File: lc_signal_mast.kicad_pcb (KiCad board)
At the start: 2 copper layers, 100.4 x 93.2 mm, 64 parts, among them J1 Conn_01x04_Male, J2 Conn_01x04_Male

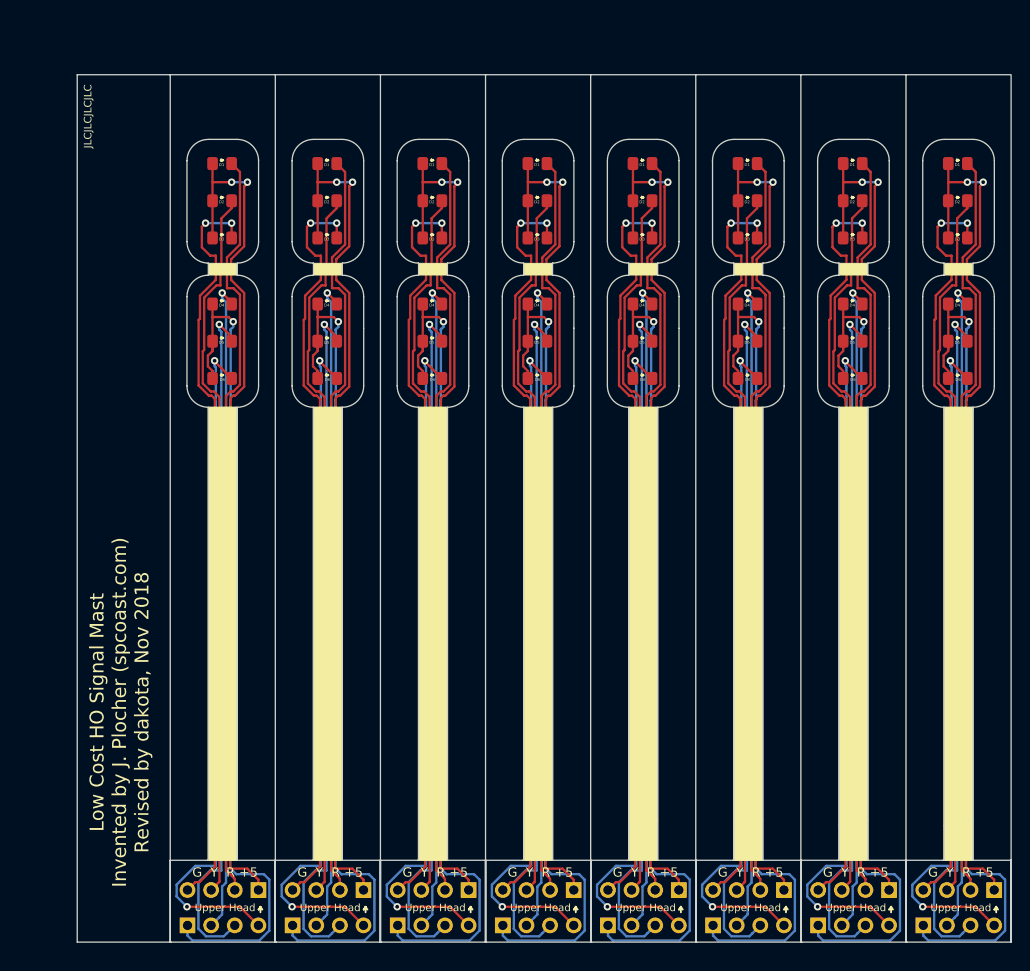
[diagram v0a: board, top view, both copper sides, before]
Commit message: Stagger headers on the bottom; swap R/G LED footprints.
Fixes #6 and #9.
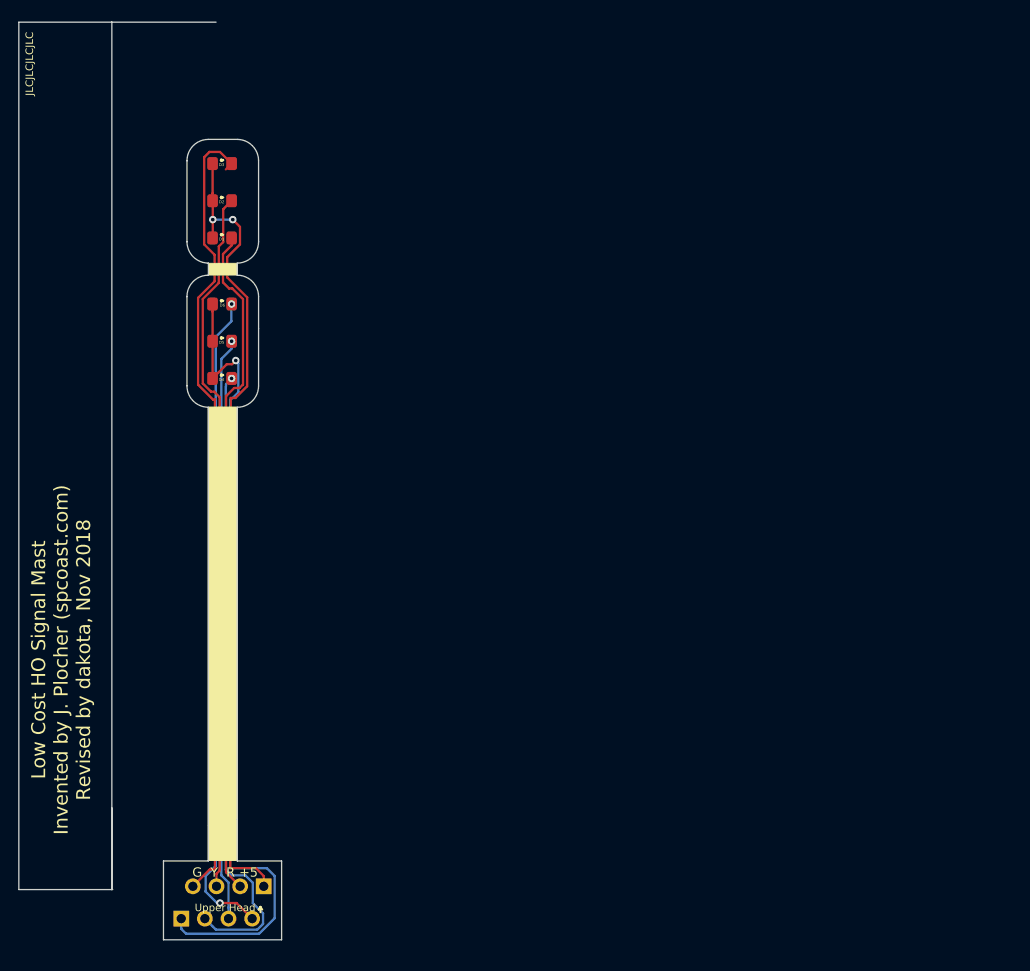
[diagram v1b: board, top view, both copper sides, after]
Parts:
- removed the D1 at (116.0, 74.2)
- removed the D1 at (104.7, 74.2)
- removed the D1 at (93.4, 74.2)
- removed the D1 at (82.1, 74.2)
- removed the D1 at (70.8, 74.2)
- removed the D1 at (59.5, 74.2)
- removed the D1 at (48.2, 74.2)
- removed the D1 at (36.9, 74.2)
- removed the D2 at (116.0, 78.2)
- removed the D2 at (104.7, 78.2)
- removed the D2 at (93.4, 78.2)
- removed the D2 at (82.1, 78.2)
- removed the D2 at (70.8, 78.2)
- removed the D2 at (59.5, 78.2)
- removed the D2 at (48.2, 78.2)
- removed the D3 at (116.0, 82.2)
- removed the D3 at (104.7, 82.2)
- removed the D3 at (93.4, 82.2)
- removed the D3 at (82.1, 82.2)
- removed the D3 at (70.8, 82.2)
- removed the D3 at (59.5, 82.2)
- removed the D3 at (48.2, 82.2)
- removed the D4 at (116.0, 89.3)
- removed the D4 at (104.7, 89.3)
- removed the D4 at (93.4, 89.3)
- removed the D4 at (82.1, 89.3)
- removed the D4 at (70.8, 89.3)
- removed the D4 at (59.5, 89.3)
- removed the D4 at (48.2, 89.3)
- removed the D4 at (36.9, 89.3)
- removed the D5 at (116.0, 93.3)
- removed the D5 at (104.7, 93.3)
- removed the D5 at (93.4, 93.3)
- removed the D5 at (82.1, 93.3)
- removed the D5 at (70.8, 93.3)
- removed the D5 at (59.5, 93.3)
- removed the D5 at (48.2, 93.3)
- removed the D6 at (116.0, 97.3)
- removed the D6 at (104.7, 97.3)
- removed the D6 at (93.4, 97.3)
- removed the D6 at (82.1, 97.3)
- removed the D6 at (70.8, 97.3)
- removed the D6 at (59.5, 97.3)
- removed the D6 at (48.2, 97.3)
- removed the J1 at (119.9, 152.3)
- removed the J1 at (108.6, 152.3)
- removed the J1 at (97.3, 152.3)
- removed the J1 at (86.0, 152.3)
- removed the J1 at (74.7, 152.3)
- removed the J1 at (63.4, 152.3)
- removed the J1 at (52.1, 152.3)
- removed the J2 at (112.3, 156.2)
- removed the J2 at (101.0, 156.2)
- removed the J2 at (89.7, 156.2)
- removed the J2 at (78.4, 156.2)
- removed the J2 at (67.1, 156.2)
- removed the J2 at (55.8, 156.2)
- removed the J2 at (44.5, 156.2)
- added D1: LED, dakota_footprints:LED_0805_HandSolder_Pretty, F.Cu at (36.9, 82.2)
- added D4: LED, dakota_footprints:LED_0805_HandSolder_Pretty, F.Cu at (36.9, 97.3)
- moved D3 8.00 mm to (36.9, 74.2)
- moved D6 8.00 mm to (36.9, 89.3)
- moved J2 0.99 mm to (32.5, 155.4)
- moved J1 0.70 mm to (41.4, 151.9)
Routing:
- net /+5V_1: track 737.6 -> 87.8 mm, vias 16 -> 2
- net /+5V_2: track 731.3 -> 88.1 mm, vias 8 -> 1
- net /RED1: track 649.8 -> 72.9 mm
- net /GREEN1: track 643.7 -> 86.4 mm, vias 16 -> 0
- net /YELLOW1: track 615.7 -> 76.1 mm
- net /YELLOW2: track 590.9 -> 63.5 mm, vias 8 -> 1
- net /GREEN2: track 591.8 -> 70.7 mm, vias 16 -> 2
- net /RED2: track 563.4 -> 69.0 mm, vias 8 -> 1
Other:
- board size 100.4 x 93.2 mm -> 28.2 x 98.6 mm
